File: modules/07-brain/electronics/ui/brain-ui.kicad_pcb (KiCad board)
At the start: 2 copper layers, 58 x 110 mm, 54 parts, among them J1 Conn_02x03_Odd_Even, J2 Conn_01x02, J3 Conn_01x02, J4 Conn_02x02_Odd_Even, J5 Conn_02x03_Odd_Even, J6 Conn_02x02_Odd_Even, J7 Conn_02x05_Odd_Even, J8 Conn_02x03_Odd_Even, Q1 2N3904, Q2 2N3904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

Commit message: Verfied JLCPCB for Brain 1.0
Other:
- board text added: "HM-07 BRAIN V1.0 2025 DEC"
- board text added: "SHMØERGH MODULEUR"
- board text removed: "HM-07 BRAIN V0.1 2025 SEP"
- board text removed: "SHMØERGH HOG MODULEUR"

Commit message: Added pull-down resistor for Brain pulse input
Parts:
- added R2: 10k, Shmoergh_Custom_Footprints:R_Axial_DIN0207_L6.3mm_D2.5mm_P7.62mm_Horizontal, F.Cu at (162.3, 122.5)
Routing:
- net PULSE_IN: track 140.4 -> 144.2 mm
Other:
- board text added: "HM-07 BRAIN V1.1 2025 JAN"
- board text removed: "HM-07 BRAIN V1.0 2025 DEC"

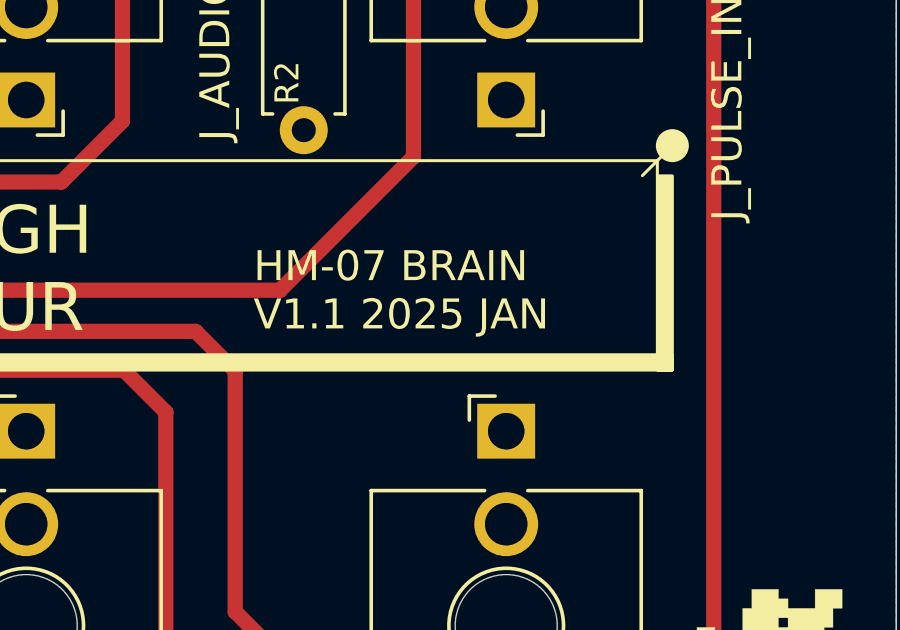
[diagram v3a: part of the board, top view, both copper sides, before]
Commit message: Updated Brain silkscreen bug
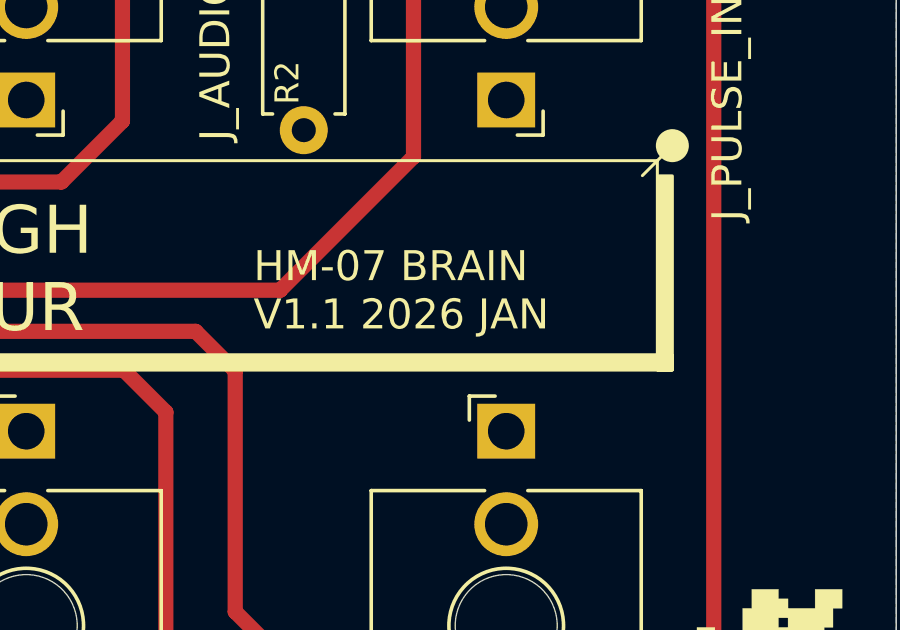
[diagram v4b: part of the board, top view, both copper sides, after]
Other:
- board text added: "HM-07 BRAIN V1.1 2026 JAN"
- board text removed: "HM-07 BRAIN V1.1 2025 JAN"
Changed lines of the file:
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@@
 		)
 	)
-	(gr_text "HM-07 BRAIN\nV1.1 2025 JAN"
+	(gr_text "HM-07 BRAIN\nV1.1 2026 JAN"
 		(at 160.576 129.217 0)
 		(layer "F.SilkS")
@@
 			(justify left bottom)
 		)
-		(render_cache "HM-07 BRAIN\nV1.1 2025 JAN" 0
+		(render_cache "HM-07 BRAIN\nV1.1 2026 JAN" 0
 			(polygon
 				(pts
@@
 			(polygon
 				(pts
-					(xy 167.823418 128.028812) (xy 167.823418 128.537936) (xy 168.332481 128.537936) (xy 168.332481 128.410686)
-					(xy 167.950668 128.410686) (xy 167.950668 128.156124) (xy 168.459792 128.156124) (xy 168.459792 128.028812)
+					(xy 167.950668 128.028812) (xy 167.950668 128.156124) (xy 168.332481 128.156124) (xy 168.332481 128.028812)
+				)
+			)
+			(polygon
+				(pts
+					(xy 167.823418 128.156124) (xy 167.823418 128.919749) (xy 167.950668 128.919749) (xy 167.950668 128.537936)
+					(xy 168.332481 128.537936) (xy 168.332481 128.410686) (xy 167.950668 128.410686) (xy 167.950668 128.156124)
 				)
 			)
@@
 			(polygon
 				(pts
-					(xy 168.332481 128.919749) (xy 167.950668 128.919749) (xy 167.950668 129.047) (xy 168.332481 129.047)
-				)
-			)
-			(polygon
-				(pts
-					(xy 167.950668 128.919749) (xy 167.950668 128.792498) (xy 167.823418 128.792498) (xy 167.823418 128.919749)
-				)
-			)
+					(xy 167.950668 128.919749) (xy 167.950668 129.047) (xy 168.332481 129.047) (xy 168.332481 128.919749)
+				)
+			)
+			(polygon
+				(pts
+					(xy 168.332481 128.156124) (xy 168.332481 128.283374) (xy 168.459792 128.283374) (xy 168.459792 128.156124)
+				)
+			)

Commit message: Updated Stereo Jack product number on Brain MIDI
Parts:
- J_MIDI1: value PJ398SM-STEREO -> PJ366ST
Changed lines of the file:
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@@
 			)
 		)
-		(property "Value" "PJ398SM-STEREO"
+		(property "Value" "PJ366ST"
 			(at 0 -1.48 180)
 			(layer "F.Fab")
@@
 			)
 		)
-		(property "Part no." "PJ398SM"
+		(property "Part no." "PJ366ST Stereo"
 			(at 0 0 0)
 			(unlocked yes)
@@
 			(at 0 0 0)
 			(unlocked yes)
+			(layer "F.Fab")
+			(hide yes)
+			(effects
+				(font
+					(size 1 1)
+					(thickness 0.15)
+				)
+			)
+		)
+		(property "Part No." ""
+			(at 0 0 0)
+			(unlocked yes)

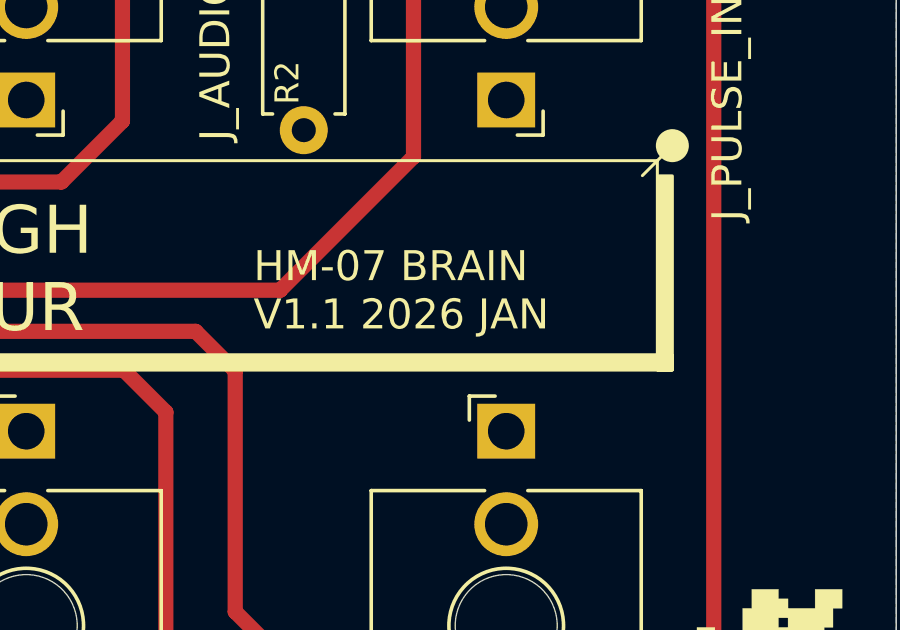
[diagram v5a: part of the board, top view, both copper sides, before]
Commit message: KiCAD version update - Brain
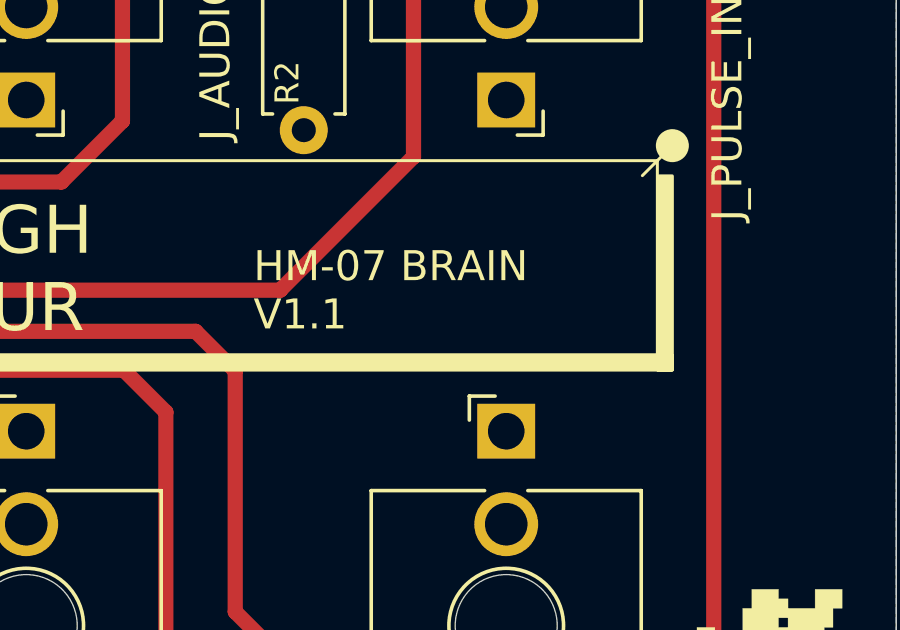
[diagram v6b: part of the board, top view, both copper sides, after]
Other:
- board text added: "HM-07 BRAIN V1.1"
- board text removed: "HM-07 BRAIN V1.1 2026 JAN"
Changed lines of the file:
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@@
 		)
 	)
-	(gr_text "HM-07 BRAIN\nV1.1 2026 JAN"
+	(gr_text "HM-07 BRAIN\nV1.1"
 		(at 160.576 129.217 0)
 		(layer "F.SilkS")
@@
 			(justify left bottom)
 		)
-		(render_cache "HM-07 BRAIN\nV1.1 2026 JAN" 0
+		(render_cache "HM-07 BRAIN\nV1.1" 0
 			(polygon
 				(pts
@@
 				)
 			)
-			(polygon
-				(pts
-					(xy 165.153355 128.792498) (xy 165.153355 129.047) (xy 165.789729 129.047) (xy 165.789729 128.919749)
-					(xy 165.280605 128.919749) (xy 165.280605 128.792498)
-				)
-			)
-			(polygon
-				(pts
-					(xy 165.662418 128.156124) (xy 165.662418 128.028812) (xy 165.280605 128.028812) (xy 165.280605 128.156124)
-				)
-			)
-			(polygon
-				(pts
-					(xy 165.662418 128.156124) (xy 165.662418 128.410686) (xy 165.789729 128.410686) (xy 165.789729 128.156124)
-				)
-			)
-			(polygon
-				(pts
-					(xy 165.280605 128.665187) (xy 165.280605 128.792498) (xy 165.407917 128.792498) (xy 165.407917 128.665187)
-				)
-			)
-			(polygon
-				(pts
-					(xy 165.153355 128.156124) (xy 165.153355 128.283374) (xy 165.280605 128.283374) (xy 165.280605 128.156124)
-				)
-			)
-			(polygon
-				(pts
-					(xy 165.535167 128.410686) (xy 165.535167 128.537936) (xy 165.662418 128.537936) (xy 165.662418 128.410686)
-				)
-			)
-			(polygon
-				(pts
-					(xy 165.407917 128.537936) (xy 165.407917 128.665187) (xy 165.535167 128.665187) (xy 165.535167 128.537936)
-				)
-			)
-			(polygon
-				(pts
-					(xy 166.043376 128.156124) (xy 166.043376 128.919749) (xy 166.170626 128.919749) (xy 166.170626 128.665187)
-					(xy 166.297938 128.665187) (xy 166.297938 128.537936) (xy 166.170626 128.537936) (xy 166.170626 128.156124)
-				)
-			)
-			(polygon
-				(pts
-					(xy 166.170626 128.919749) (xy 166.170626 129.047) (xy 166.552439 129.047) (xy 166.552439 128.919749)
-				)
-			)
-			(polygon
-				(pts
-					(xy 166.170626 128.028812) (xy 166.170626 128.156124) (xy 166.552439 128.156124) (xy 166.552439 128.028812)
-				)
-			)
-			(polygon
-				(pts
-					(xy 166.552439 128.156124) (xy 166.552439 128.283374) (xy 166.425188 128.283374) (xy 166.425188 128.410686)
-					(xy 166.552439 128.410686) (xy 166.552439 128.919749) (xy 166.67975 128.919749) (xy 166.67975 128.156124)
-				)
-			)
-			(polygon
-				(pts
-					(xy 166.297938 128.410686) (xy 166.297938 128.537936) (xy 166.425188 128.537936) (xy 166.425188 128.410686)
-				)
-			)
-			(polygon
-				(pts
-					(xy 166.933397 128.792498) (xy 166.933397 129.047) (xy 167.569771 129.047) (xy 167.569771 128.919749)
-					(xy 167.060647 128.919749) (xy 167.060647 128.792498)
-				)
-			)
-			(polygon
-				(pts
-					(xy 167.44246 128.156124) (xy 167.44246 128.028812) (xy 167.060647 128.028812) (xy 167.060647 128.156124)
-				)
-			)
-			(polygon
-				(pts
-					(xy 167.44246 128.156124) (xy 167.44246 128.410686) (xy 167.569771 128.410686) (xy 167.569771 128.156124)
-				)
-			)
-			(polygon
-				(pts
-					(xy 167.060647 128.665187) (xy 167.060647 128.792498) (xy 167.187959 128.792498) (xy 167.187959 128.665187)
-				)
-			)
-			(polygon
-				(pts
-					(xy 166.933397 128.156124) (xy 166.933397 128.283374) (xy 167.060647 128.283374) (xy 167.060647 128.156124)
-				)
-			)
-			(polygon
-				(pts
-					(xy 167.315209 128.410686) (xy 167.315209 128.537936) (xy 167.44246 128.537936) (xy 167.44246 128.410686)
-				)
-			)
-			(polygon
-				(pts
-					(xy 167.187959 128.537936) (xy 167.187959 128.665187) (xy 167.315209 128.665187) (xy 167.315209 128.537936)
-				)
-			)
-			(polygon
-				(pts
-					(xy 167.950668 128.028812) (xy 167.950668 128.156124) (xy 168.332481 128.156124) (xy 168.332481 128.028812)
-				)
-			)
-			(polygon
-				(pts
-					(xy 167.823418 128.156124) (xy 167.823418 128.919749) (xy 167.950668 128.919749) (xy 167.950668 128.537936)
-					(xy 168.332481 128.537936) (xy 168.332481 128.410686) (xy 167.950668 128.410686) (xy 167.950668 128.156124)
-				)
-			)
-			(polygon
-				(pts
-					(xy 168.332481 128.537936) (xy 168.332481 128.919749) (xy 168.459792 128.919749) (xy 168.459792 128.537936)
-				)
-			)
-			(polygon
-				(pts
-					(xy 167.950668 128.919749) (xy 167.950668 129.047) (xy 168.332481 129.047) (xy 168.332481 128.919749)
-				)
-			)
-			(polygon
-				(pts
-					(xy 168.332481 128.156124) (xy 168.332481 128.283374) (xy 168.459792 128.283374) (xy 168.459792 128.156124)
-				)
-			)
-			(polygon
-				(pts
-					(xy 169.73071 128.919749) (xy 169.73071 128.792498) (xy 169.603459 128.792498) (xy 169.603459 128.919749)
-				)
-			)
-			(polygon
-				(pts
-					(xy 169.73071 128.919749) (xy 169.73071 129.047) (xy 170.112523 129.047) (xy 170.112523 128.919749)
-				)
-			)
-			(polygon
-				(pts
-					(xy 170.112523 128.156124) (xy 170.112523 128.919749) (xy 170.239834 128.919749) (xy 170.239834 128.028812)
-					(xy 169.858021 128.028812) (xy 169.858021 128.156124)
-				)
-			)
-			(polygon
-				(pts
-					(xy 170.49348 128.283374) (xy 170.49348 129.047) (xy 170.620731 129.047) (xy 170.620731 128.665187)
-					(xy 171.002543 128.665187) (xy 171.002543 129.047) (xy 171.129855 129.047) (xy 171.129855 128.283374)
-					(xy 171.002543 128.283374) (xy 171.002543 128.537936) (xy 170.620731 128.537936) (xy 170.620731 128.283374)
-				)
-			)
-			(polygon
-				(pts
-					(xy 170.748042 128.028812) (xy 170.748042 128.156124) (xy 170.875293 128.156124) (xy 170.875293 128.028812)
-				)
-			)
-			(polygon
-				(pts
-					(xy 170.620731 128.156124) (xy 170.620731 128.283374) (xy 170.748042 128.283374) (xy 170.748042 128.156124)
-				)
-			)
-			(polygon
-				(pts
-					(xy 170.875293 128.156124) (xy 170.875293 128.283374) (xy 171.002543 128.283374) (xy 171.002543 128.156124)
-				)
-			)
-			(polygon
-				(pts
-					(xy 171.383501 128.028812) (xy 171.383501 129.047) (xy 171.510752 129.047) (xy 171.510752 128.410686)
-					(xy 171.638063 128.410686) (xy 171.638063 128.283374) (xy 171.510752 128.283374) (xy 171.510752 128.028812)
-				)
-			)
-			(polygon
-				(pts
-					(xy 171.892564 128.665187) (xy 171.892564 129.047) (xy 172.019876 129.047) (xy 172.019876 128.028812)
-					(xy 171.892564 128.028812) (xy 171.892564 128.537936) (xy 171.765314 128.537936) (xy 171.765314 128.665187)
-				)
-			)
-			(polygon
-				(pts
-					(xy 171.765314 128.537936) (xy 171.765314 128.410686) (xy 171.638063 128.410686) (xy 171.638063 128.537936)
-				)
-			)

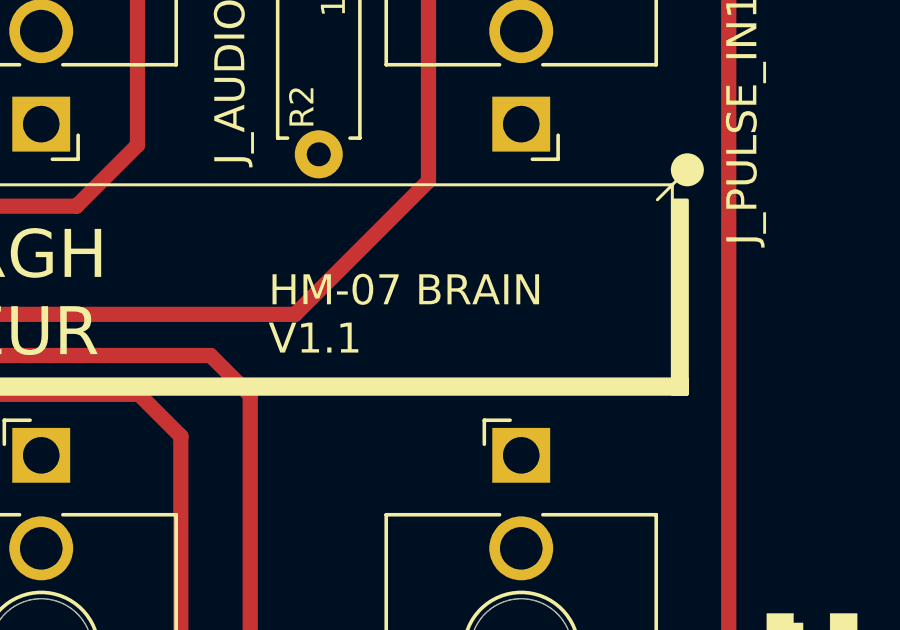
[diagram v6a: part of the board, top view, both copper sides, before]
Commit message: Updated rev. number in Brain
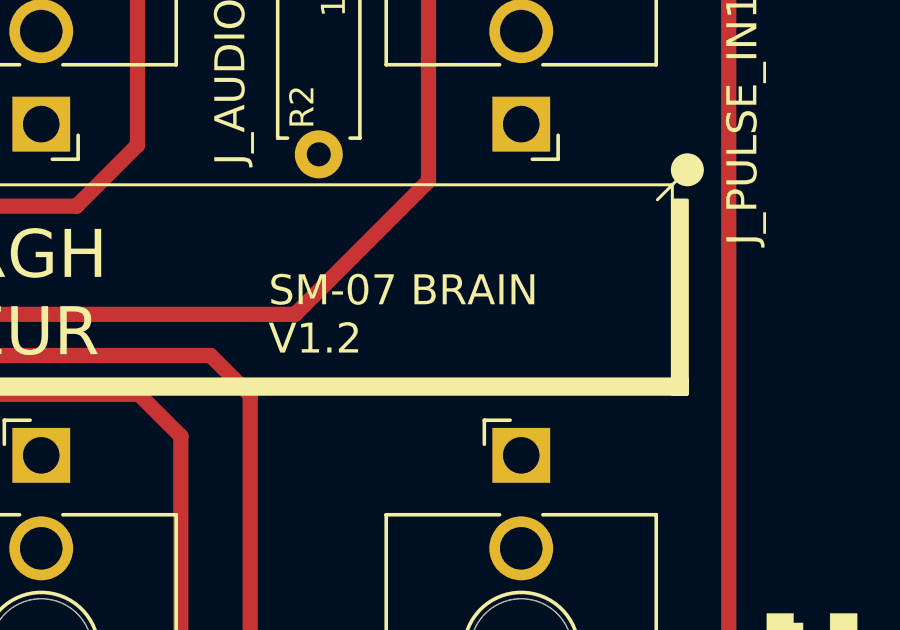
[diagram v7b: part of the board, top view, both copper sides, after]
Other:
- board text added: "SM-07 BRAIN V1.2"
- board text removed: "HM-07 BRAIN V1.1"
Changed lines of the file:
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@@
 		)
 	)
-	(gr_text "HM-07 BRAIN\nV1.1"
+	(gr_text "SM-07 BRAIN\nV1.2"
 		(at 160.576 129.217 0)
 		(layer "F.SilkS")
@@
 			(justify left bottom)
 		)
-		(render_cache "HM-07 BRAIN\nV1.1" 0
-			(polygon
-				(pts
-					(xy 160.70325 126.348812) (xy 160.70325 127.367) (xy 160.830501 127.367) (xy 160.830501 126.857936)
-					(xy 161.212313 126.857936) (xy 161.212313 127.367) (xy 161.339625 127.367) (xy 161.339625 126.348812)
-					(xy 161.212313 126.348812) (xy 161.212313 126.730686) (xy 160.830501 126.730686) (xy 160.830501 126.348812)
+		(render_cache "SM-07 BRAIN\nV1.2" 0
+			(polygon
+				(pts
+					(xy 160.70325 126.476124) (xy 160.70325 126.730686) (xy 160.830501 126.730686) (xy 160.830501 126.476124)
+				)
+			)
+			(polygon
+				(pts
+					(xy 160.830501 126.730686) (xy 160.830501 126.857936) (xy 161.212313 126.857936) (xy 161.212313 126.730686)
+				)
+			)
+			(polygon
+				(pts
+					(xy 161.212313 127.239749) (xy 160.830501 127.239749) (xy 160.830501 127.367) (xy 161.212313 127.367)
+				)
+			)
+			(polygon
+				(pts
+					(xy 160.830501 127.239749) (xy 160.830501 127.112498) (xy 160.70325 127.112498) (xy 160.70325 127.239749)
+				)
+			)
+			(polygon
+				(pts
+					(xy 161.212313 126.857936) (xy 161.212313 127.239749) (xy 161.339625 127.239749) (xy 161.339625 126.857936)
+				)
+			)
+			(polygon
+				(pts
+					(xy 160.830501 126.348812) (xy 160.830501 126.476124) (xy 161.212313 126.476124) (xy 161.212313 126.348812)
+				)
+			)
+			(polygon
+				(pts
+					(xy 161.212313 126.476124) (xy 161.212313 126.603374) (xy 161.339625 126.603374) (xy 161.339625 126.476124)
 				)
 			)
@@
 			(polygon
 				(pts
-					(xy 163.627875 128.283374) (xy 163.627875 128.919749) (xy 163.373313 128.919749) (xy 163.373313 129.047)
-					(xy 164.009688 129.047) (xy 164.009688 128.919749) (xy 163.755125 128.919749) (xy 163.755125 128.028812)
-					(xy 163.627875 128.028812) (xy 163.627875 128.156124) (xy 163.373313 128.156124) (xy 163.373313 128.283374)
-				)
-			)
+					(xy 163.373313 128.792498) (xy 163.373313 129.047) (xy 164.009688 129.047) (xy 164.009688 128.919749)
+					(xy 163.500563 128.919749) (xy 163.500563 128.792498)
+				)
+			)
+			(polygon
+				(pts
+					(xy 163.882376 128.156124) (xy 163.882376 128.028812) (xy 163.500563 128.028812) (xy 163.500563 128.156124)
+				)
+			)
+			(polygon
+				(pts
+					(xy 163.882376 128.156124) (xy 163.882376 128.410686) (xy 164.009688 128.410686) (xy 164.009688 128.156124)
+				)
+			)
+			(polygon
+				(pts
+					(xy 163.500563 128.665187) (xy 163.500563 128.792498) (xy 163.627875 128.792498) (xy 163.627875 128.665187)
+				)
+			)
+			(polygon
+				(pts
+					(xy 163.373313 128.156124) (xy 163.373313 128.283374) (xy 163.500563 128.283374) (xy 163.500563 128.156124)
+				)
+			)
+			(polygon
+				(pts
+					(xy 163.755125 128.410686) (xy 163.755125 128.537936) (xy 163.882376 128.537936) (xy 163.882376 128.410686)
+				)
+			)
+			(polygon
+				(pts
+					(xy 163.627875 128.537936) (xy 163.627875 128.665187) (xy 163.755125 128.665187) (xy 163.755125 128.537936)
+				)
+			)

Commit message: Moduleur Hardware v1.1 update
PSU v1.1

- Replaced 1N4001 with 1N5822 Schottky diode for overall better performance (faster switch, less temperature dissipation, better surge behavior, ~0.2V voltage drop)
- Added 1.5KE36A TVS at DC jack for ESD protection

VCA v1.3

- Added test resistors to VCA output and VCA input

Brain v1.3

- Added testing resistor and protection diode to pulse output on UI board
- Updated Mounting Hole H3 to connect to GND so it's not necessary to use wired connection to ground the front and backpanel.
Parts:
- added D7: 1N4148, Diode_THT:D_DO-35_SOD27_P7.62mm_Horizontal, F.Cu at (159.5, 140.0)
- added R15: 0, Shmoergh_Custom_Footprints:R_Axial_DIN0207_L6.3mm_D2.5mm_P7.62mm_Horizontal, F.Cu at (162.3, 132.4)
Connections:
- H3 pad 1: (no net) -> GND
- J_PULSE_OUT1 pad T: PULSE_OUT -> Net-(J_PULSE_OUT1-PadT)
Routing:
- net PULSE_OUT: track 142.4 -> 124.8 mm
- net Net-(J_PULSE_OUT1-PadT): track 0.00 -> 9.77 mm
- net Net-(D7-K): track 0.00 -> 8.80 mm
- net +12V: track 222.2 -> 224.3 mm
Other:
- board text added: "SM-07 BRAIN V1.3"
- board text removed: "SM-07 BRAIN V1.2"
